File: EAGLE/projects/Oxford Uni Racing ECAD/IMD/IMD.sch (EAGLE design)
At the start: 7 parts, among them IC1 LM2901N, J1 T821108A1S100CEU, K1 RT444012

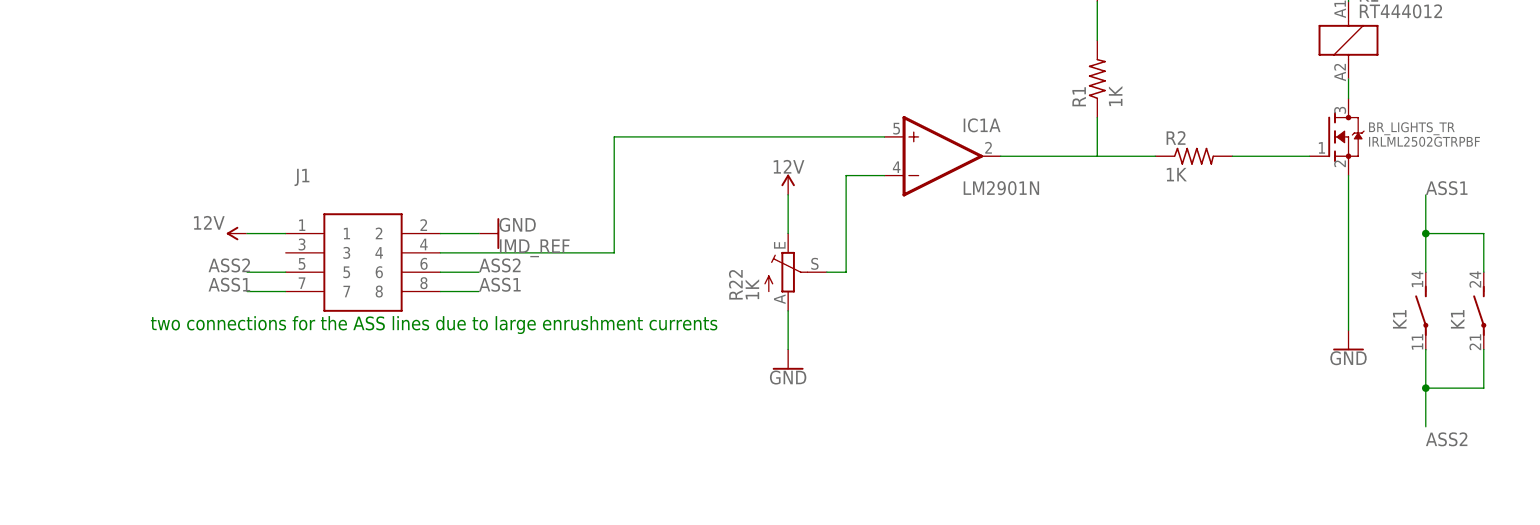
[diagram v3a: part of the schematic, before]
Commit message: replaced fuses with correct sized ones
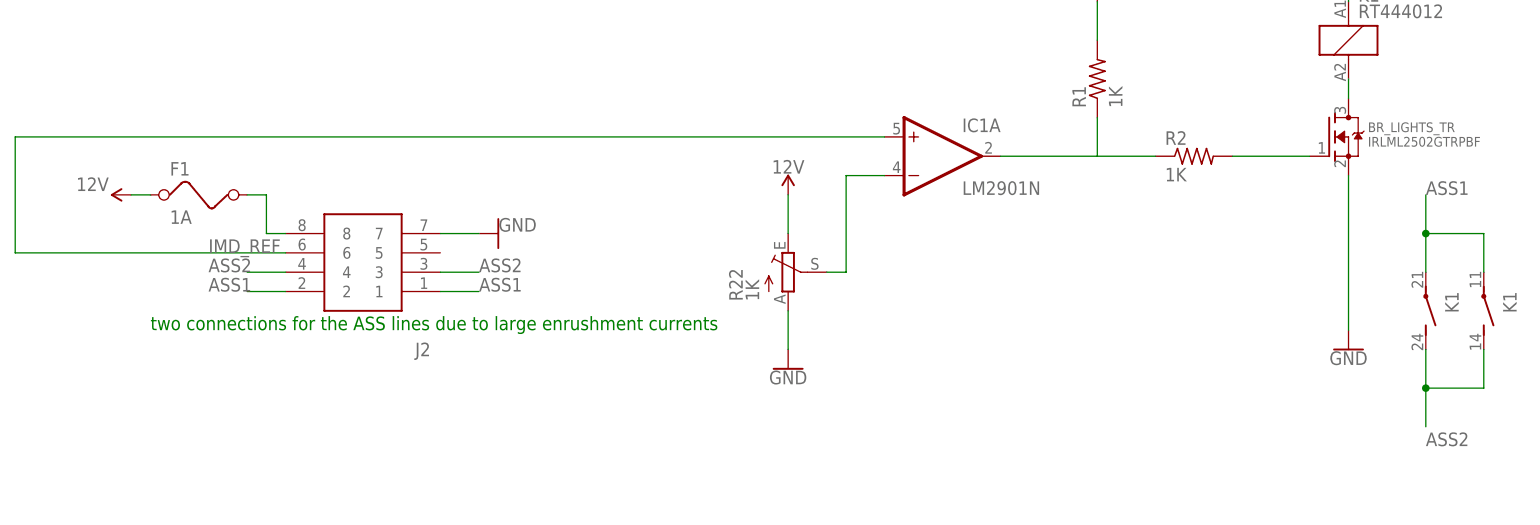
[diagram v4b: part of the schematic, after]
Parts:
- removed J1: T821108A1S100CEU, T821108A1S100CEU:T821108A1S100CEU
- added F1: 1A, special:FUSE
- added J2: T821108A1S100CEU, T821108A1S100CEU:T821108A1S100CEU
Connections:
- new net N$2: F1.2, J2.8
- net 12V: now also F1.1; no longer J1.1
- net ASS1: now also J2.1, J2.2, K12.P, K13.P; no longer J1.7, J1.8, K12.S, K13.S
- net ASS2: now also J2.3, J2.4, K12.S, K13.S; no longer J1.5, J1.6, K12.P, K13.P
- net GND: now also J2.7; no longer J1.2
- net IMD_REF: now also J2.6; no longer J1.4
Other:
- moved on the sheet: K1
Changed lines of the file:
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@@
 </classes>
 <parts>
-<part name="J1" library="T821108A1S100CEU" deviceset="T821108A1S100CEU" device="" value=""/>
 <part name="R22" library="pot" library_urn="urn:adsk.eagle:library:331" deviceset="TRIM_EU-" device="B90P" package3d_urn="urn:adsk.eagle:package:22714/1" value="1K"/>
 <part name="IC1" library="linear" library_urn="urn:adsk.eagle:library:262" deviceset="LM2901" device="N" package3d_urn="urn:adsk.eagle:package:16407/2"/>
@@
 <part name="R2" library="adafruit" library_urn="urn:adsk.eagle:library:420" deviceset="R-US_" device="0204/7" package3d_urn="urn:adsk.eagle:package:6240596/1" value="1K"/>
 <part name="GND20" library="SparkFun-PowerSymbols" library_urn="urn:adsk.eagle:library:530" deviceset="GND" device=""/>
+<part name="F1" library="special" library_urn="urn:adsk.eagle:library:367" deviceset="FUSE" device="" package3d_urn="urn:adsk.eagle:package:26650/1" value="1A"/>
+<part name="J2" library="T821108A1S100CEU" deviceset="T821108A1S100CEU" device="" value=""/>
 </parts>
 <sheets>
@@
 </plain>
 <instances>
-<instance part="J1" gate="G$1" x="38.1" y="27.94" smashed="yes">
-<attribute name="NAME" x="39.37" y="35.56" size="1.778" layer="95" align="center-left"/>
-<attribute name="VALUE" x="39.37" y="33.02" size="1.778" layer="96" align="center-left"/>
-</instance>
 <instance part="R22" gate="1" x="104.14" y="22.86" smashed="yes">
 <attribute name="NAME" x="98.171" y="19.05" size="1.778" layer="95" rot="R90"/>
@@
 <attribute name="PART" x="179.07" y="58.42" size="1.778" layer="95"/>
 </instance>
-<instance part="K1" gate="2" x="187.96" y="17.78" smashed="yes">
-<attribute name="PART" x="185.42" y="15.24" size="1.778" layer="95" rot="R90"/>
-</instance>
-<instance part="K1" gate="3" x="195.58" y="17.78" smashed="yes">
-<attribute name="PART" x="193.04" y="15.24" size="1.778" layer="95" rot="R90"/>
-</instance>
-<instance part="SUPPLY1" gate="G$1" x="33.02" y="27.94" smashed="yes" rot="R90">
-<attribute name="VALUE" x="27.94" y="30.226" size="1.778" layer="96" rot="R180" align="bottom-center"/>
+<instance part="K1" gate="2" x="195.58" y="17.78" smashed="yes" rot="R180">
+<attribute name="PART" x="198.12" y="20.32" size="1.778" layer="95" rot="R270"/>
+</instance>
+<instance part="K1" gate="3" x="187.96" y="17.78" smashed="yes" rot="R180">
+<attribute name="PART" x="190.5" y="20.32" size="1.778" layer="95" rot="R270"/>
+</instance>
+<instance part="SUPPLY1" gate="G$1" x="17.78" y="33.02" smashed="yes" rot="R90">
+<attribute name="VALUE" x="12.7" y="35.306" size="1.778" layer="96" rot="R180" align="bottom-center"/>
 </instance>
 <instance part="SUPPLY2" gate="G$1" x="177.8" y="60.96" smashed="yes">
@@
 <instance part="GND20" gate="1" x="177.8" y="12.7" smashed="yes">
 <attribute name="VALUE" x="177.8" y="12.446" size="1.778" layer="96" align="top-center"/>
+</instance>
+<instance part="F1" gate="G$1" x="27.94" y="33.02" smashed="yes">
+<attribute name="NAME" x="22.86" y="35.56" size="1.778" layer="95"/>
+<attribute name="VALUE" x="22.86" y="29.21" size="1.778" layer="96"/>
+</instance>
+<instance part="J2" gate="G$1" x="58.42" y="20.32" smashed="yes" rot="R180">
+<attribute name="NAME" x="57.15" y="12.7" size="1.778" layer="95" rot="R180" align="center-left"/>
+<attribute name="VALUE" x="57.15" y="15.24" size="1.778" layer="96" rot="R180" align="center-left"/>
 </instance>
 </instances>
@@
 </segment>
 <segment>
-<pinref part="J1" gate="G$1" pin="2"/>
 <pinref part="GND1" gate="1" pin="GND"/>
 <wire x1="58.42" y1="27.94" x2="63.5" y2="27.94" width="0.1524" layer="91"/>
+<pinref part="J2" gate="G$1" pin="7"/>
 </segment>
 <segment>
@@
 </segment>
 <segment>
-<pinref part="J1" gate="G$1" pin="1"/>
-<pinref part="SUPPLY1" gate="G$1" pin="12V"/>
-<wire x1="38.1" y1="27.94" x2="33.02" y2="27.94" width="0.1524" layer="91"/>
-</segment>
-<segment>
 <pinref part="SUPPLY4" gate="G$1" pin="12V"/>
 <pinref part="R22" gate="1" pin="E"/>
 <wire x1="104.14" y1="33.02" x2="104.14" y2="27.94" width="0.1524" layer="91"/>
 </segment>
+<segment>
+<pinref part="F1" gate="G$1" pin="1"/>
+<pinref part="SUPPLY1" gate="G$1" pin="12V"/>
+<wire x1="20.32" y1="33.02" x2="17.78" y2="33.02" width="0.1524" layer="91"/>
+</segment>
 </net>
 <net name="ASS1" class="0">
 <segment>
-<pinref part="K1" gate="2" pin="S"/>
-<wire x1="187.96" y1="22.86" x2="187.96" y2="27.94" width="0.1524" layer="91"/>
 <wire x1="187.96" y1="27.94" x2="195.58" y2="27.94" width="0.1524" layer="91"/>
-<pinref part="K1" gate="3" pin="S"/>
-<wire x1="195.58" y1="27.94" x2="195.58" y2="22.86" width="0.1524" layer="91"/>
 <wire x1="187.96" y1="27.94" x2="187.96" y2="33.02" width="0.1524" layer="91"/>
+<label x="187.96" y="33.02" size="1.778" layer="95"/>
+<pinref part="K1" gate="2" pin="P"/>
+<wire x1="195.58" y1="22.86" x2="195.58" y2="27.94" width="0.1524" layer="91"/>
+<pinref part="K1" gate="3" pin="P"/>
+<wire x1="187.96" y1="27.94" x2="187.96" y2="22.86" width="0.1524" layer="91"/>
 <junction x="187.96" y="27.94"/>
-<label x="187.96" y="33.02" size="1.778" layer="95"/>
-</segment>
-<segment>
-<pinref part="J1" gate="G$1" pin="7"/>
+</segment>
+<segment>
 <wire x1="38.1" y1="20.32" x2="33.02" y2="20.32" width="0.1524" layer="91"/>
 <label x="27.94" y="20.32" size="1.778" layer="95"/>
-</segment>
-<segment>
-<pinref part="J1" gate="G$1" pin="8"/>
+<pinref part="J2" gate="G$1" pin="2"/>
+</segment>
+<segment>
 <wire x1="63.5" y1="20.32" x2="58.42" y2="20.32" width="0.1524" layer="91"/>
 <label x="63.5" y="20.32" size="1.778" layer="95"/>
+<pinref part="J2" gate="G$1" pin="1"/>
 </segment>
 </net>
 <net name="ASS2" class="0">
 <segment>
-<pinref part="K1" gate="2" pin="P"/>
+<wire x1="187.96" y1="7.62" x2="195.58" y2="7.62" width="0.1524" layer="91"/>
+<wire x1="187.96" y1="7.62" x2="187.96" y2="2.54" width="0.1524" layer="91"/>
+<label x="187.96" y="0" size="1.778" layer="95"/>
+<pinref part="K1" gate="3" pin="S"/>
 <wire x1="187.96" y1="12.7" x2="187.96" y2="7.62" width="0.1524" layer="91"/>
-<wire x1="187.96" y1="7.62" x2="195.58" y2="7.62" width="0.1524" layer="91"/>
-<pinref part="K1" gate="3" pin="P"/>
-<wire x1="195.58" y1="7.62" x2="195.58" y2="12.7" width="0.1524" layer="91"/>
-<wire x1="187.96" y1="7.62" x2="187.96" y2="2.54" width="0.1524" layer="91"/>
 <junction x="187.96" y="7.62"/>
-<label x="187.96" y="0" size="1.778" layer="95"/>
-</segment>
-<segment>
-<pinref part="J1" gate="G$1" pin="6"/>
+<pinref part="K1" gate="2" pin="S"/>
+<wire x1="195.58" y1="12.7" x2="195.58" y2="7.62" width="0.1524" layer="91"/>
+</segment>
+<segment>
 <wire x1="58.42" y1="22.86" x2="63.5" y2="22.86" width="0.1524" layer="91"/>
 <label x="63.5" y="22.86" size="1.778" layer="95"/>
-</segment>
-<segment>
-<pinref part="J1" gate="G$1" pin="5"/>
+<pinref part="J2" gate="G$1" pin="3"/>
+</segment>
+<segment>
 <wire x1="38.1" y1="22.86" x2="33.02" y2="22.86" width="0.1524" layer="91"/>
 <label x="27.94" y="22.86" size="1.778" layer="95"/>
+<pinref part="J2" gate="G$1" pin="4"/>
 </segment>
 </net>
@@
 <net name="IMD_REF" class="0">
 <segment>
-<pinref part="J1" gate="G$1" pin="4"/>
-<wire x1="58.42" y1="25.4" x2="81.28" y2="25.4" width="0.1524" layer="91"/>
 <pinref part="IC1" gate="A" pin="+IN"/>
-<wire x1="81.28" y1="25.4" x2="81.28" y2="40.64" width="0.1524" layer="91"/>
-<wire x1="81.28" y1="40.64" x2="116.84" y2="40.64" width="0.1524" layer="91"/>
-<label x="66.04" y="25.4" size="1.778" layer="95"/>
+<label x="27.94" y="25.4" size="1.778" layer="95"/>
+<pinref part="J2" gate="G$1" pin="6"/>
+<wire x1="38.1" y1="25.4" x2="2.54" y2="25.4" width="0.1524" layer="91"/>
+<wire x1="2.54" y1="25.4" x2="2.54" y2="40.64" width="0.1524" layer="91"/>
+<wire x1="2.54" y1="40.64" x2="116.84" y2="40.64" width="0.1524" layer="91"/>
 </segment>
 </net>
@@
 </segment>
 </net>
+<net name="N$2" class="0">
+<segment>
+<pinref part="J2" gate="G$1" pin="8"/>
+<wire x1="38.1" y1="27.94" x2="35.56" y2="27.94" width="0.1524" layer="91"/>
+<wire x1="35.56" y1="27.94" x2="35.56" y2="33.02" width="0.1524" layer="91"/>
+<pinref part="F1" gate="G$1" pin="2"/>
+<wire x1="35.56" y1="33.02" x2="33.02" y2="33.02" width="0.1524" layer="91"/>
+</segment>
+</net>

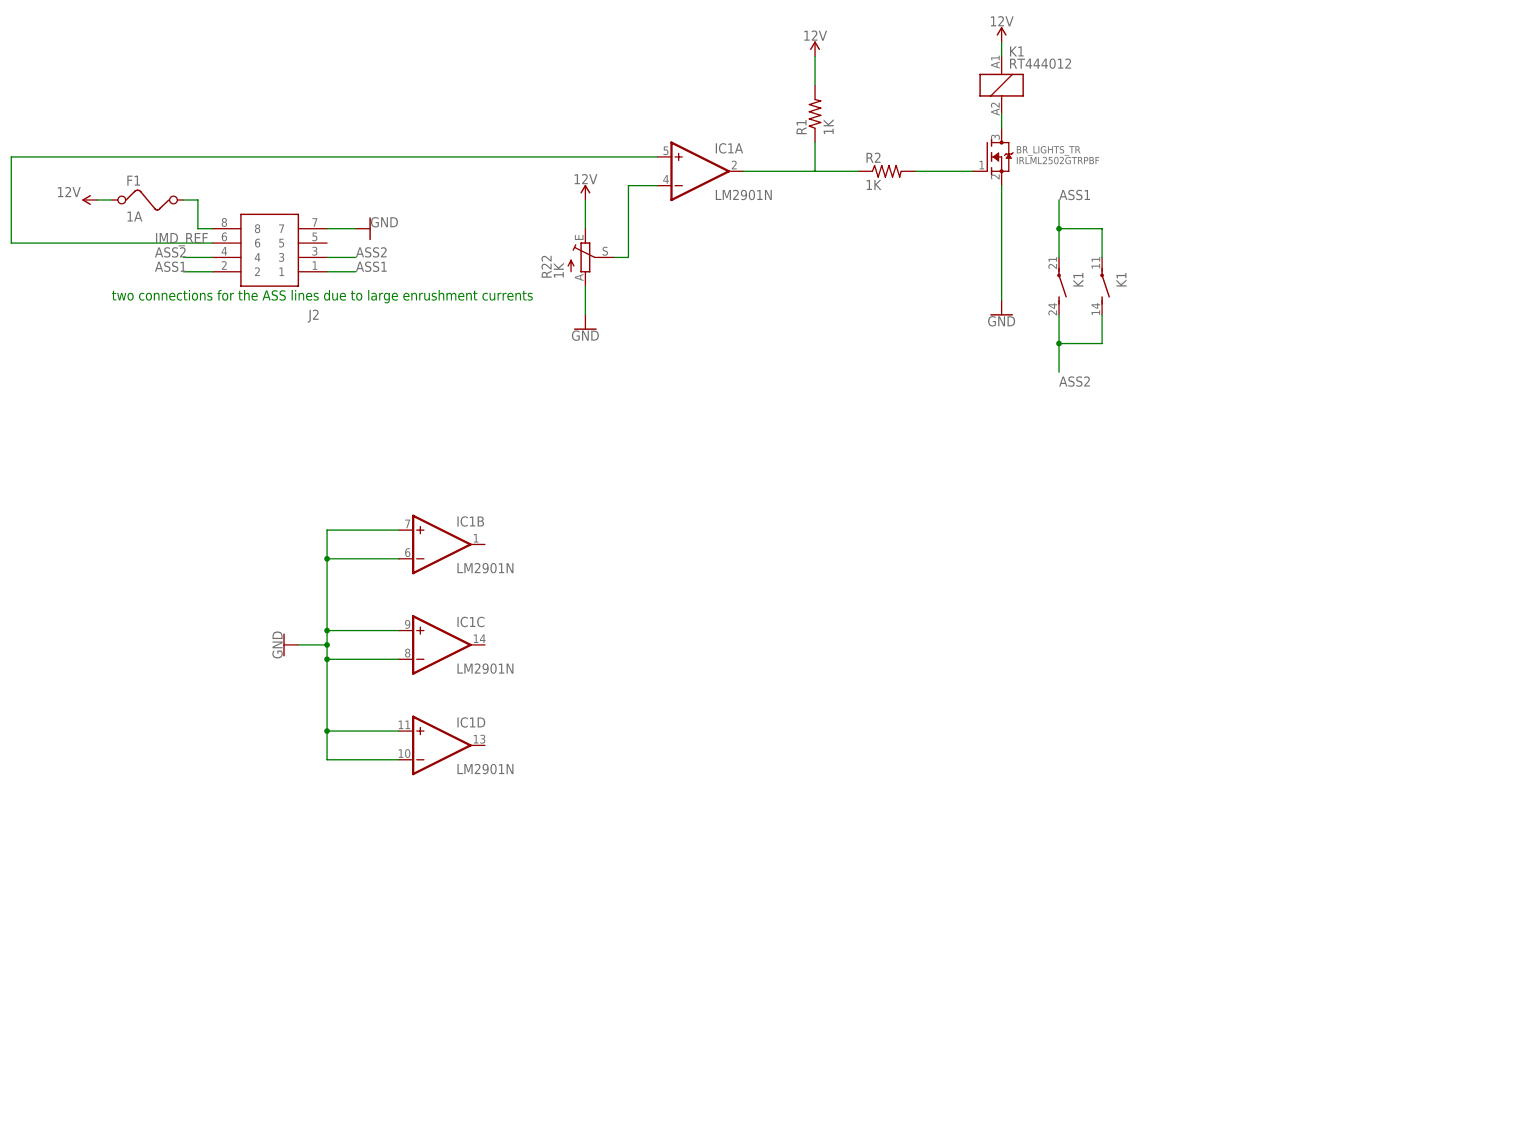
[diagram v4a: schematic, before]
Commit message: First iteration of TSAL schematic
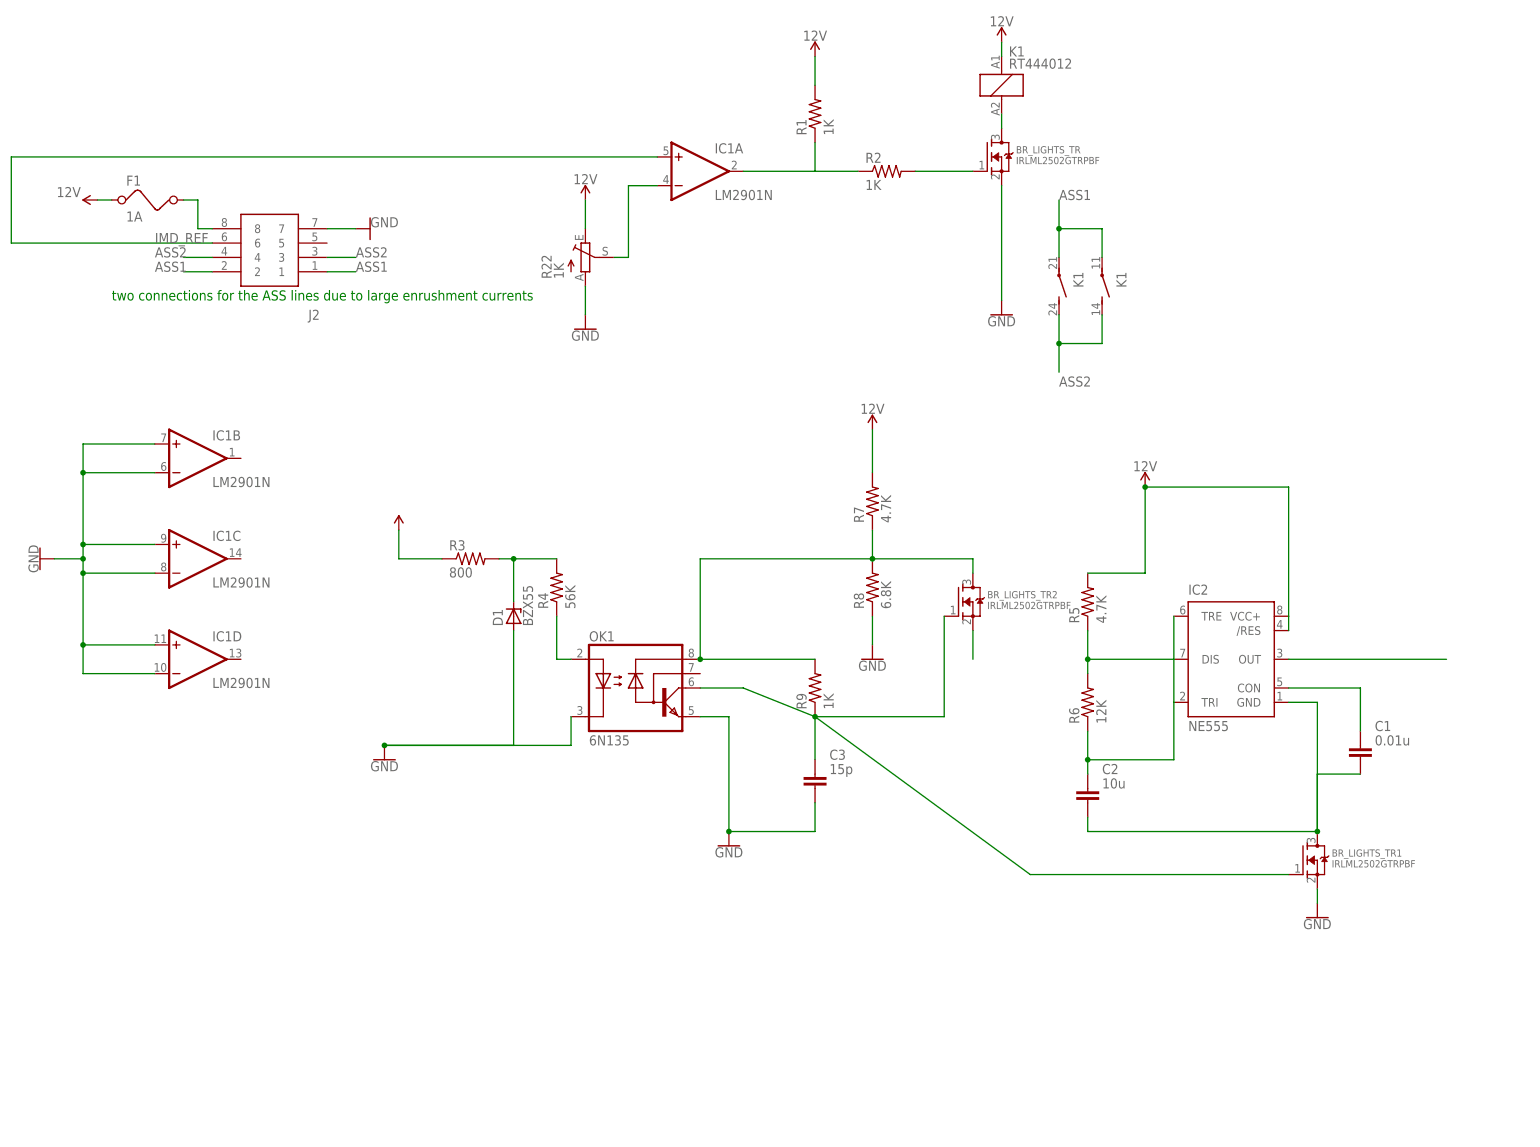
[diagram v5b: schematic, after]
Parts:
- added BR_LIGHTS_TR1, BR_LIGHTS_TR2: IRLML2502GTRPBF, adafruit:MOSFET-NREFLOW
- added C1: 0.01u, ngspice-simulation:C
- added C2: 10u, ngspice-simulation:C
- added C3: 15p, ngspice-simulation:C
- added D1: BZX55, diode:BZX55
- added IC2: NE555, st-microelectronics:NE555
- added OK1: 6N135, optocoupler:6N135
- added R3: 800, adafruit:R-US_0204/7
- added R4: 56K, adafruit:R-US_0204/7
- added R5, R7: 4.7K, adafruit:R-US_0204/7
- added R6: 12K, adafruit:R-US_0204/7
- added R8: 6.8K, adafruit:R-US_0204/7
- added R9: 1K, adafruit:R-US_0204/7
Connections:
- new net N$10: C1.1, IC2.CON
- new net N$11: IC2.DIS, R5.1, R6.2
- new net N$12: C2.1, IC2.TRE, IC2.TRI, R6.1
- new net N$13: BR_LIGHTS_TR2.S
- new net N$14: BR_LIGHTS_TR1.D, C1.2, C2.2, IC2.GND
- new net N$16: BR_LIGHTS_TR2.D, OK1.VCC, R7.1, R8.2, R9.2
- new net N$17: BR_LIGHTS_TR1.G, BR_LIGHTS_TR2.G, C3.1, OK1.VO, R9.1
- new net N$5: R3.1
- new net N$7: OK1.A, R4.1
- new net N$8: D1.C, R3.2, R4.2
- new net N$9: IC2.OUT
- net 12V: now also IC2./RES, IC2.VCC+, R5.2, R7.2
- net GND: now also BR_LIGHTS_TR1.S, C3.2, D1.A, OK1.C, OK1.GND, R8.1
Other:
- moved on the sheet: IC1B, IC1C, IC1D
